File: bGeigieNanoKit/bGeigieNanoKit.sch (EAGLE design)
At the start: 36 parts, among them T1 2SC1815

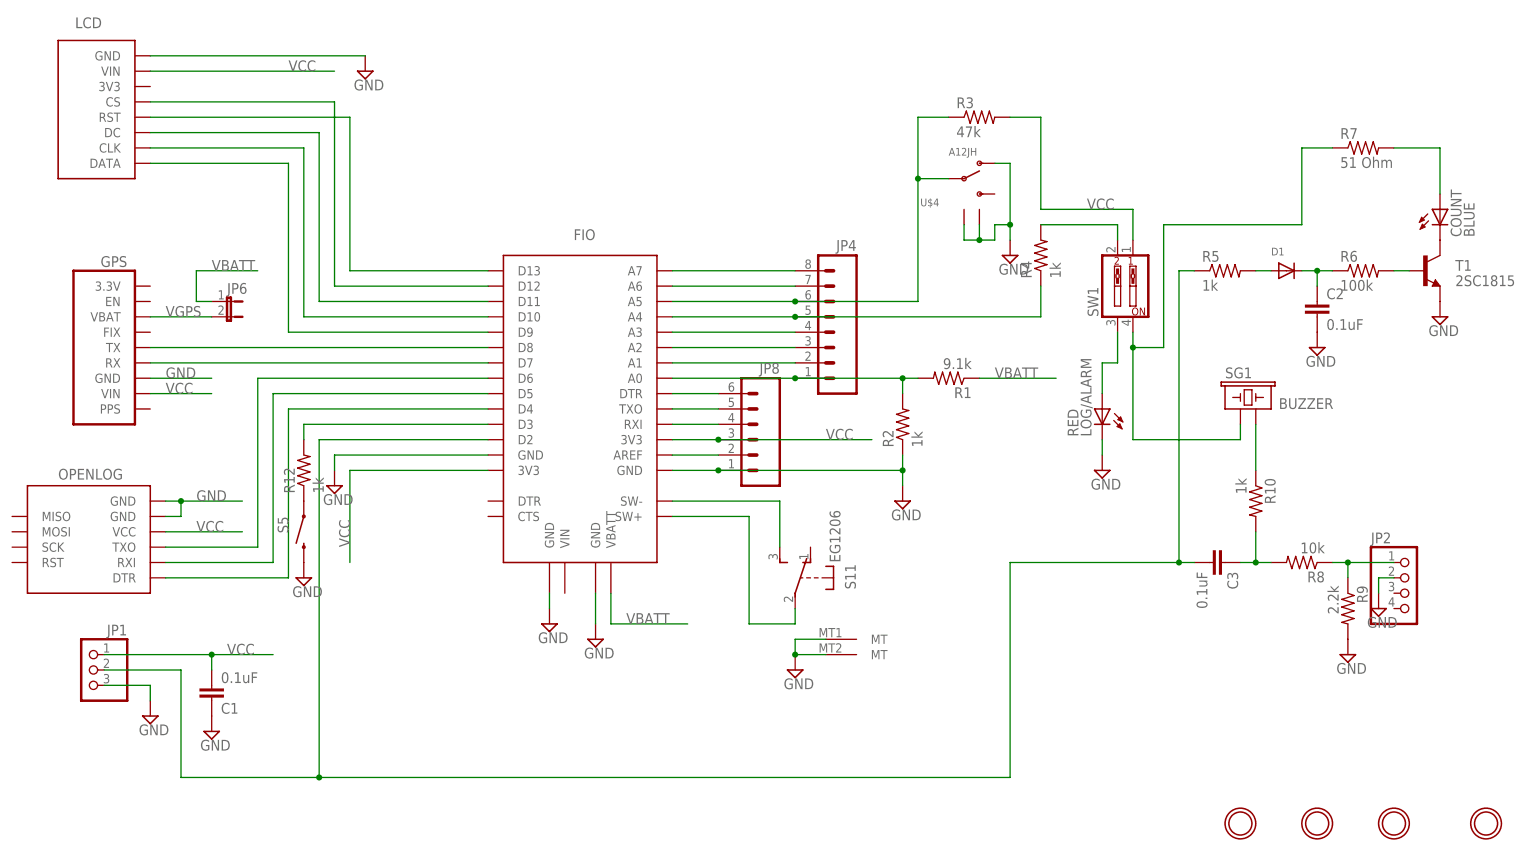
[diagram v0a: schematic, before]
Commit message: Changed R8 to 47k and and R9 to 4.7k and fixed some overlaying text.
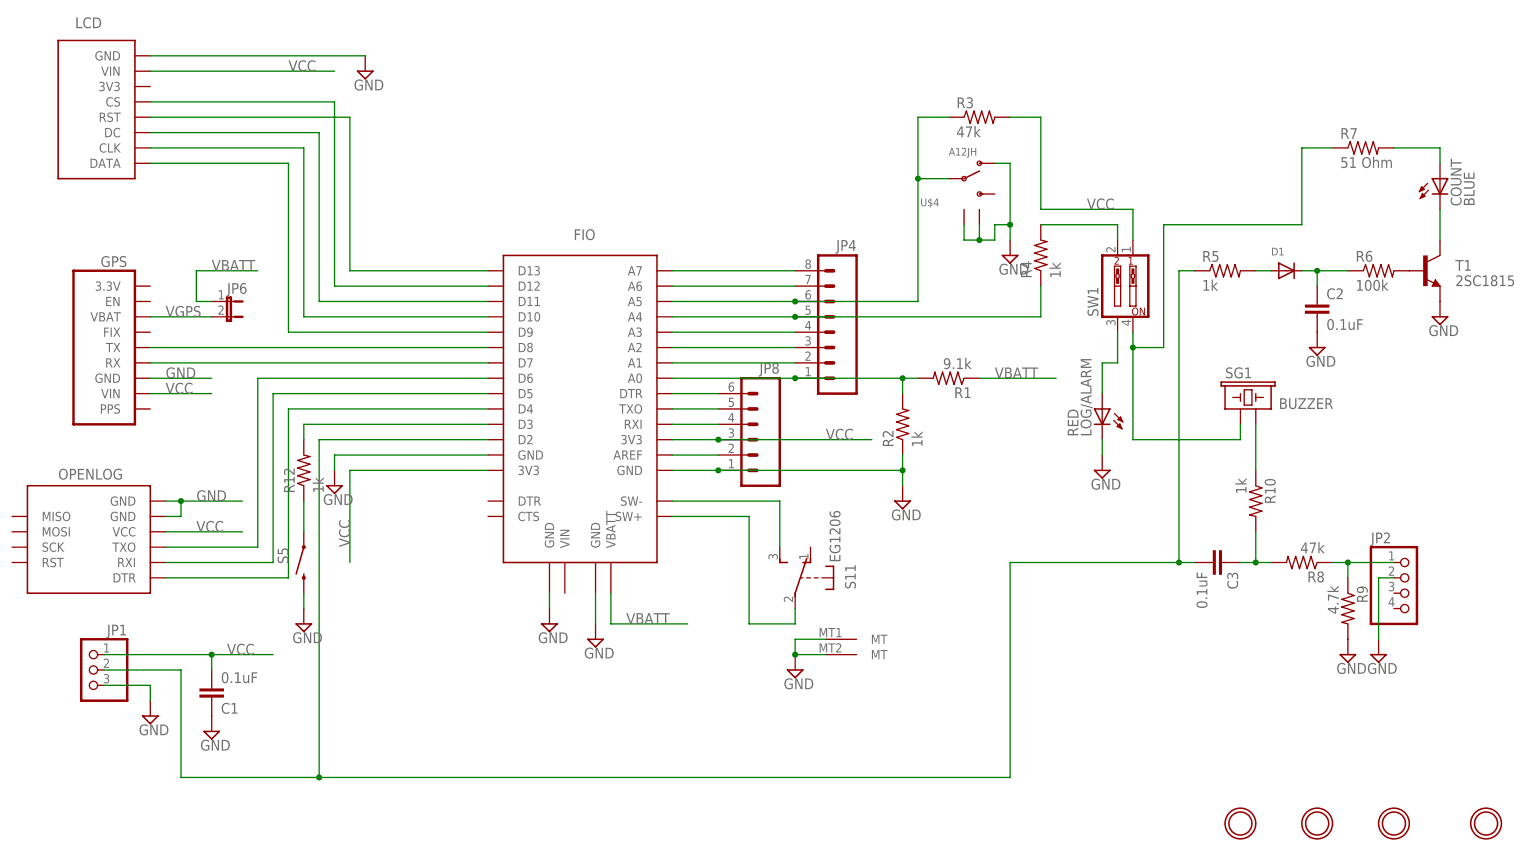
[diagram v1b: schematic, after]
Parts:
- R8: value 10k -> 47k
- R9: value 2.2k -> 4.7k
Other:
- moved on the sheet: COUNT, R6, S5
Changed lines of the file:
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@@
 <part name="R6" library="rcl" deviceset="R-US_" device="0207/10" value="100k"/>
 <part name="R7" library="rcl" deviceset="R-US_" device="0207/10" value="51 Ohm"/>
-<part name="R8" library="rcl" deviceset="R-US_" device="0207/10" value="10k"/>
-<part name="R9" library="rcl" deviceset="R-US_" device="0207/10" value="2.2k"/>
+<part name="R8" library="rcl" deviceset="R-US_" device="0207/10" value="47k"/>
+<part name="R9" library="rcl" deviceset="R-US_" device="0207/10" value="4.7k"/>
 <part name="R10" library="rcl" deviceset="R-US_" device="0207/10" value="1k"/>
 <part name="SUPPLY1" library="supply2" deviceset="GND" device=""/>
@@
 <instances>
 <instance part="GPS" gate="U$1" x="20.32" y="109.22" rot="MR0"/>
-<instance part="COUNT" gate="G$1" x="241.3" y="132.08"/>
+<instance part="COUNT" gate="G$1" x="241.3" y="137.16"/>
 <instance part="LOG/ALARM" gate="G$1" x="185.42" y="99.06" rot="MR0"/>
 <instance part="JP1" gate="A" x="17.78" y="55.88" rot="MR0"/>
-<instance part="S5" gate="G$1" x="53.34" y="78.74" rot="MR270"/>
+<instance part="S5" gate="G$1" x="53.34" y="73.66" rot="MR270"/>
 <instance part="SG1" gate="G$1" x="208.28" y="99.06"/>
 <instance part="FIO" gate="U$1" x="99.06" y="104.14" smashed="yes" rot="MR180">
@@
 <instance part="R4" gate="G$1" x="175.26" y="124.46" rot="R90"/>
 <instance part="R5" gate="G$1" x="205.74" y="121.92"/>
-<instance part="R6" gate="G$1" x="228.6" y="121.92"/>
+<instance part="R6" gate="G$1" x="231.14" y="121.92"/>
 <instance part="R7" gate="G$1" x="228.6" y="142.24"/>
 <instance part="R8" gate="G$1" x="218.44" y="73.66" rot="R180"/>
@@
 </instance>
 <instance part="SUPPLY11" gate="GND" x="226.06" y="58.42"/>
-<instance part="SUPPLY12" gate="GND" x="231.14" y="66.04"/>
+<instance part="SUPPLY12" gate="GND" x="231.14" y="58.42"/>
 <instance part="SUPPLY13" gate="GND" x="220.98" y="109.22"/>
 <instance part="SUPPLY14" gate="GND" x="241.3" y="114.3"/>
-<instance part="SUPPLY15" gate="GND" x="53.34" y="71.12"/>
+<instance part="SUPPLY15" gate="GND" x="53.34" y="63.5"/>
 <instance part="OPENLOG" gate="U$1" x="17.78" y="76.2"/>
 <instance part="SW1" gate="G$1" x="187.96" y="119.38" rot="R90"/>
@@
 <pinref part="SUPPLY12" gate="GND" pin="GND"/>
 <wire x1="233.68" y1="71.12" x2="231.14" y2="71.12" width="0.1524" layer="91"/>
-<wire x1="231.14" y1="71.12" x2="231.14" y2="68.58" width="0.1524" layer="91"/>
+<wire x1="231.14" y1="71.12" x2="231.14" y2="60.96" width="0.1524" layer="91"/>
 <pinref part="JP2" gate="A" pin="2"/>
 </segment>
@@
 <pinref part="SUPPLY15" gate="GND" pin="GND"/>
 <pinref part="S5" gate="G$1" pin="2"/>
+<wire x1="53.34" y1="66.04" x2="53.34" y2="68.58" width="0.1524" layer="91"/>
 </segment>
 <segment>
@@
 <wire x1="218.44" y1="121.92" x2="220.98" y2="121.92" width="0.1524" layer="91"/>
 <pinref part="C2" gate="G$1" pin="1"/>
-<wire x1="220.98" y1="121.92" x2="223.52" y2="121.92" width="0.1524" layer="91"/>
+<wire x1="220.98" y1="121.92" x2="226.06" y2="121.92" width="0.1524" layer="91"/>
 <wire x1="220.98" y1="119.38" x2="220.98" y2="121.92" width="0.1524" layer="91"/>
 <junction x="220.98" y="121.92"/>
@@
 <pinref part="R6" gate="G$1" pin="2"/>
 <pinref part="T1" gate="G$1" pin="B"/>
-<wire x1="233.68" y1="121.92" x2="236.22" y2="121.92" width="0.1524" layer="91"/>
 </segment>
 </net>
@@
 <pinref part="T1" gate="G$1" pin="C"/>
 <pinref part="COUNT" gate="G$1" pin="C"/>
+<wire x1="241.3" y1="132.08" x2="241.3" y2="127" width="0.1524" layer="91"/>
 </segment>
 </net>
@@
 <pinref part="COUNT" gate="G$1" pin="A"/>
 <pinref part="R7" gate="G$1" pin="2"/>
-<wire x1="241.3" y1="134.62" x2="241.3" y2="142.24" width="0.1524" layer="91"/>
+<wire x1="241.3" y1="139.7" x2="241.3" y2="142.24" width="0.1524" layer="91"/>
 <wire x1="241.3" y1="142.24" x2="233.68" y2="142.24" width="0.1524" layer="91"/>
 </segment>
@@
 <pinref part="S5" gate="G$1" pin="1"/>
 <pinref part="R12" gate="G$1" pin="1"/>
-</segment>
-</net>
+<wire x1="53.34" y1="78.74" x2="53.34" y2="83.82" width="0.1524" layer="91"/>
+</segment>
+</net>
